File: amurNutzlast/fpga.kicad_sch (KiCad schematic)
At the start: 16 parts, among them U1 ICE40HX1K-TQ144

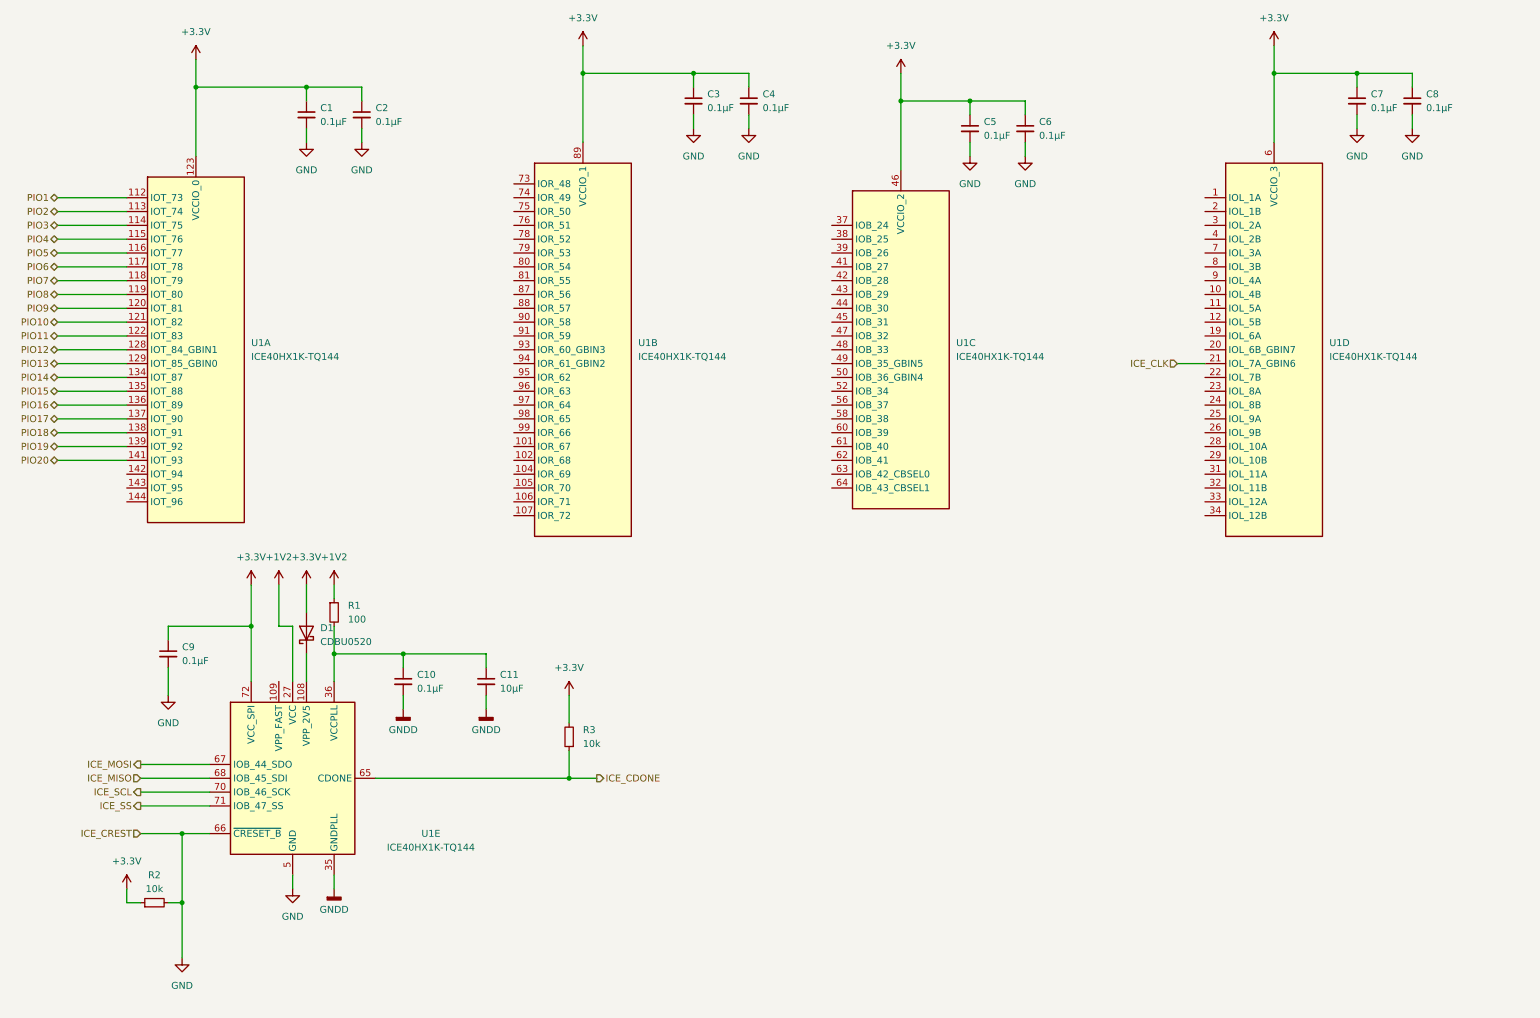
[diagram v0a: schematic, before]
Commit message: working on the FTDI design in kicad FPGA prototype board
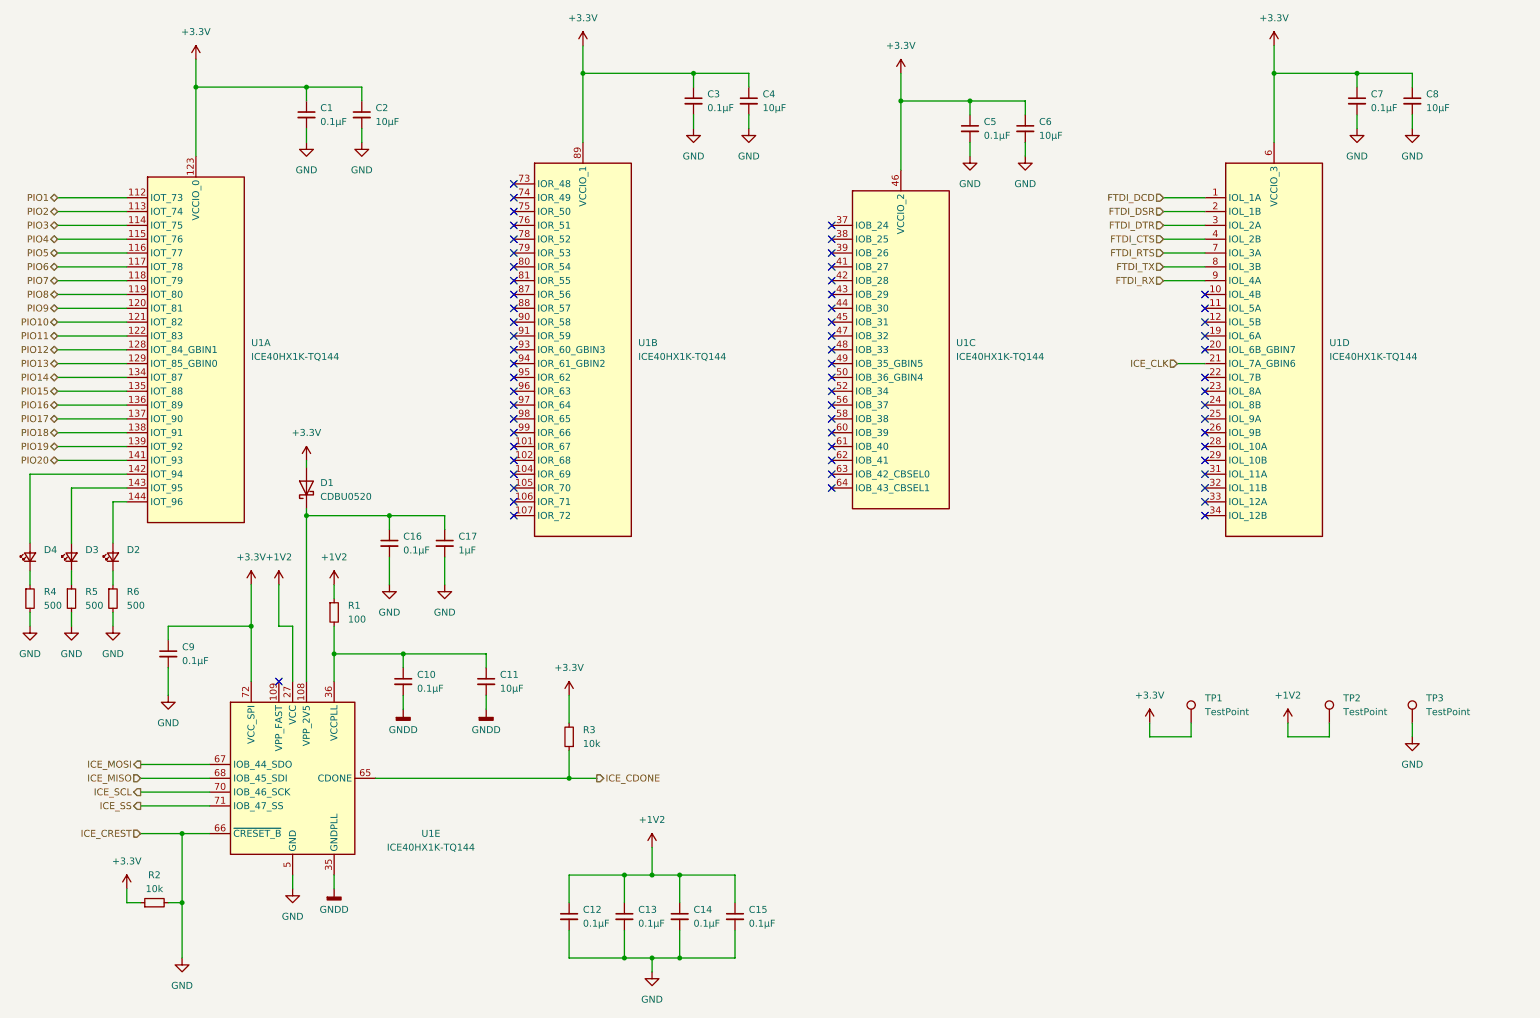
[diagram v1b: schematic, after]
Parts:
- added C12, C13, C14, C15: 0.1µF, symbol Device:C_Small
- added C16: 0.1µF, Capacitor_SMD:C_0603_1608Metric, symbol Device:C_Small
- added C17: 1µF, Capacitor_SMD:C_0603_1608Metric, symbol Device:C_Small
- added D2, D3, D4: LED_Small, LED_SMD:LED_0603_1608Metric, symbol Device:LED_Small
- added R4, R5, R6: 500, Resistor_SMD:R_0603_1608Metric, symbol Device:R_Small
- added TP1, TP2, TP3: TestPoint, TestPoint:TestPoint_Bridge_Pitch2.54mm_Drill1.0mm, symbol Connector:TestPoint
- C1, C10, C11, C3, C5, C7, C9: footprint (none) -> Capacitor_SMD:C_0603_1608Metric
- C2, C4, C6, C8: value 0.1µF -> 10µF; footprint (none) -> Capacitor_SMD:C_0603_1608Metric
- R1, R2, R3: footprint (none) -> Resistor_SMD:R_0603_1608Metric
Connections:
- net +1V2: now also C12.1, C13.1, C14.1, C15.1, TP2.1
- net +3.3V: now also TP1.1
- net GND: now also C12.2, C13.2, C14.2, C15.2, C16.2, C17.2, R4.2, R5.2, R6.2, TP3.1
- net at U1.142 (IOT_94): now also D4.2 (A)
- net at U1.143 (IOT_95): now also D3.2 (A)
- net at U1.144 (IOT_96): now also D2.2 (A)
- net FTDI_DCD: now reaches U1.1 (IOL_1A)
- net FTDI_DSR: now reaches U1.2 (IOL_1B)
- net FTDI_DTR: now reaches U1.3 (IOL_2A)
- net FTDI_CTS: now reaches U1.4 (IOL_2B)
- net FTDI_RTS: now reaches U1.7 (IOL_3A)
- net FTDI_TX: now reaches U1.8 (IOL_3B)
- net FTDI_RX: now reaches U1.9 (IOL_4A)
- net at D1.1 (K), U1.108 (VPP_2V5): now also C16.1, C17.1
- new net: D3.1 (K), R5.1
- new net: D4.1 (K), R4.1
- new net: D2.1 (K), R6.1
- no-connect marks 0 -> 62
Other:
- moved on the sheet: D1

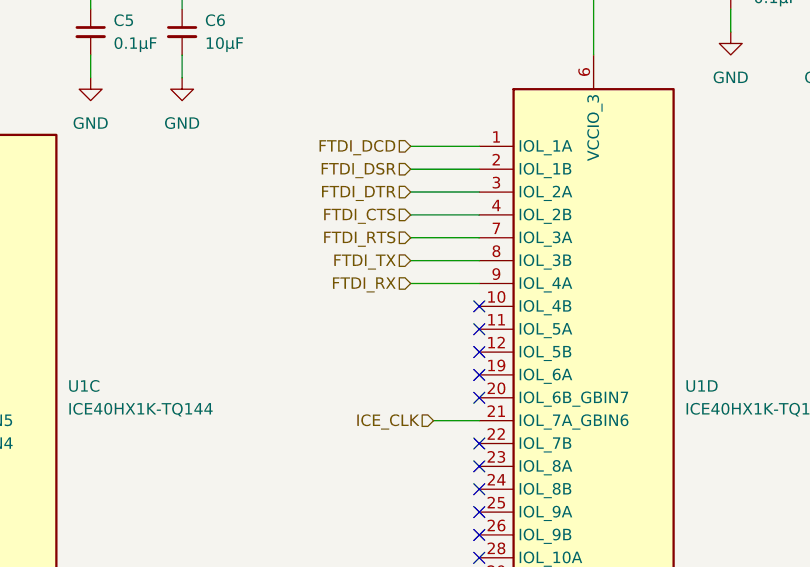
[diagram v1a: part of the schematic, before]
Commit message: ftdi schematic was added apart of the USB
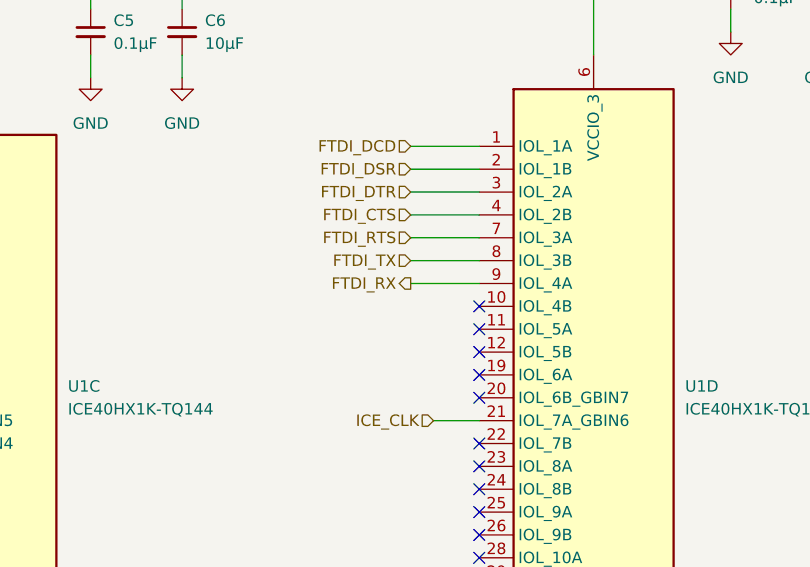
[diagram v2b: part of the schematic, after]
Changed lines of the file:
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@@
     (effects (font (size 1.27 1.27)) (justify right))
   )
-  (hierarchical_label "FTDI_RX" (shape input) (at 226.06 63.5 180) (fields_autoplaced)
+  (hierarchical_label "FTDI_RX" (shape output) (at 226.06 63.5 180) (fields_autoplaced)
     (effects (font (size 1.27 1.27)) (justify right))
   )

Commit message: finisched design schematics + pdf
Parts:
- added R26: 0, symbol Device:R_Small
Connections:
- net GND: now also R26.2; no longer R2.2, U1.66 (~{CRESET_B})
- new net ICE_CREST: R2.2, R26.1, U1.66 (~{CRESET_B})
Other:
- moved on the sheet: D1

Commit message: layout start
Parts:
- C12, C13, C14, C15: footprint (none) -> Capacitor_SMD:C_0603_1608Metric
- R26: footprint (none) -> Resistor_SMD:R_0603_1608Metric
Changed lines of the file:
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@@
       (effects (font (size 1.27 1.27)) (justify left))
     )
-    (property "Footprint" "" (at 116.84 180.34 0)
+    (property "Footprint" "Capacitor_SMD:C_0603_1608Metric" (at 116.84 180.34 0)
       (effects (font (size 1.27 1.27)) hide)
     )
@@
       (effects (font (size 1.27 1.27)) (justify left))
     )
-    (property "Footprint" "" (at 45.72 182.88 0)
+    (property "Footprint" "Resistor_SMD:R_0603_1608Metric" (at 45.72 182.88 0)
       (effects (font (size 1.27 1.27)) hide)
     )
@@
       (effects (font (size 1.27 1.27)) (justify left))
     )
-    (property "Footprint" "" (at 147.32 180.34 0)
+    (property "Footprint" "Capacitor_SMD:C_0603_1608Metric" (at 147.32 180.34 0)
       (effects (font (size 1.27 1.27)) hide)
     )
@@
       (effects (font (size 1.27 1.27)) (justify left))
     )
-    (property "Footprint" "" (at 137.16 180.34 0)
+    (property "Footprint" "Capacitor_SMD:C_0603_1608Metric" (at 137.16 180.34 0)
       (effects (font (size 1.27 1.27)) hide)
     )
@@
       (effects (font (size 1.27 1.27)) (justify left))
     )
-    (property "Footprint" "" (at 127 180.34 0)
-      (effects (font (size 1.27 1.27)) hide)
-    )
+    (property "Footprint" "Capacitor_SMD:C_0603_1608Metric" (at 127 180.34 0)
+      (effects (font (size 1.27 1.27)) hide)
+    )

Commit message: started FPGA
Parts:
- removed R26: 0, Resistor_SMD:R_0603_1608Metric, symbol Device:R_Small
- TP1, TP2, TP3: footprint TestPoint:TestPoint_Bridge_Pitch2.54mm_Drill1.0mm -> TestPoint:TestPoint_Pad_D2.5mm
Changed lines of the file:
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@@
   (junction (at 132.08 187.96) (diameter 0) (color 0 0 0 0)
-  )
-  (junction (at 45.72 177.8) (diameter 0) (color 0 0 0 0)
   )
   (junction (at 116.84 154.94) (diameter 0) (color 0 0 0 0)
@@
     (stroke (width 0) (type default))
   )
-  (wire (pts (xy 45.72 185.42) (xy 45.72 187.96))
-    (stroke (width 0) (type default))
-  )
   (wire (pts (xy 68.58 27.94) (xy 48.26 27.94))
     (stroke (width 0) (type default))
@@
   )
   (wire (pts (xy 86.36 132.08) (xy 101.6 132.08))
-    (stroke (width 0) (type default))
-  )
-  (wire (pts (xy 45.72 177.8) (xy 45.72 180.34))
     (stroke (width 0) (type default))
   )
@@
     )
   )
-  (symbol (lib_id "power:GND") (at 45.72 187.96 0) (unit 1)
-    (in_bom yes) (on_board yes) (dnp no) (fields_autoplaced)
-    (property "Reference" "#PWR023" (at 45.72 194.31 0)
-      (effects (font (size 1.27 1.27)) hide)
-    )
-    (property "Value" "GND" (at 45.72 193.04 0)
-      (effects (font (size 1.27 1.27)))
-    )
-    (property "Footprint" "" (at 45.72 187.96 0)
-      (effects (font (size 1.27 1.27)) hide)
-    )
-    (property "Datasheet" "" (at 45.72 187.96 0)
-      (effects (font (size 1.27 1.27)) hide)
-    )
-    (pin "1")
-    (instances
-      (project "amurNutzlast"
-        (path "/81bb76b1-eb1b-4eda-9d04-3f9c2ab6907c/1661226f-76a7-4703-8d64-01bff057fbe4"
-          (reference "#PWR023") (unit 1)
-        )
-      )
-    )
-  )
-  (symbol (lib_id "Device:R_Small") (at 45.72 182.88 0) (unit 1)
-    (in_bom yes) (on_board yes) (dnp no) (fields_autoplaced)
-    (property "Reference" "R26" (at 48.26 181.61 0)
-      (effects (font (size 1.27 1.27)) (justify left))
-    )
-    (property "Value" "0" (at 48.26 184.15 0)
-      (effects (font (size 1.27 1.27)) (justify left))
-    )
-    (property "Footprint" "Resistor_SMD:R_0603_1608Metric" (at 45.72 182.88 0)
-      (effects (font (size 1.27 1.27)) hide)
-    )
-    (property "Datasheet" "~" (at 45.72 182.88 0)
-      (effects (font (size 1.27 1.27)) hide)
-    )
-    (pin "1")
-    (pin "2")
-    (instances
-      (project "amurNutzlast"
-        (path "/81bb76b1-eb1b-4eda-9d04-3f9c2ab6907c/1661226f-76a7-4703-8d64-01bff057fbe4"
-          (reference "R26") (unit 1)
-        )
-      )
-    )
-  )
   (symbol (lib_id "Device:R_Small") (at 25.4 121.92 0) (unit 1)
     (in_bom yes) (on_board yes) (dnp no) (fields_autoplaced)
@@
       (effects (font (size 1.27 1.27)) (justify left))
     )
-    (property "Footprint" "TestPoint:TestPoint_Bridge_Pitch2.54mm_Drill1.0mm" (at 236.22 144.78 0)
+    (property "Footprint" "TestPoint:TestPoint_Pad_D2.5mm" (at 236.22 144.78 0)
       (effects (font (size 1.27 1.27)) hide)
     )
@@
       (effects (font (size 1.27 1.27)) (justify left))
     )
-    (property "Footprint" "TestPoint:TestPoint_Bridge_Pitch2.54mm_Drill1.0mm" (at 261.62 144.78 0)
+    (property "Footprint" "TestPoint:TestPoint_Pad_D2.5mm" (at 261.62 144.78 0)
       (effects (font (size 1.27 1.27)) hide)
     )
@@
       (effects (font (size 1.27 1.27)) (justify left))
     )
-    (property "Footprint" "TestPoint:TestPoint_Bridge_Pitch2.54mm_Drill1.0mm" (at 276.86 144.78 0)
-      (effects (font (size 1.27 1.27)) hide)
-    )
+    (property "Footprint" "TestPoint:TestPoint_Pad_D2.5mm" (at 276.86 144.78 0)
+      (effects (font (size 1.27 1.27)) hide)
+    )

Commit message: placement finished
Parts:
- added C40, C44, C46, C48: 0.1µF, Capacitor_SMD:C_0603_1608Metric, symbol Device:C_Small
- added C41, C45, C47, C49: 10µF, Capacitor_SMD:C_0603_1608Metric, symbol Device:C_Small
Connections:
- net +3.3V: now also C40.1, C41.1, C44.1, C45.1, C46.1, C47.1, C48.1, C49.1
- net GND: now also C40.2, C41.2, C44.2, C45.2, C46.2, C47.2, C48.2, C49.2
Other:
- moved on the sheet: C1, C2, C3, C4, C5, C6, C7, C8
